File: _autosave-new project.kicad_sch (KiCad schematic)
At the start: 4 parts, among them J1 LED 0.170amps, J2 Tractive Battery

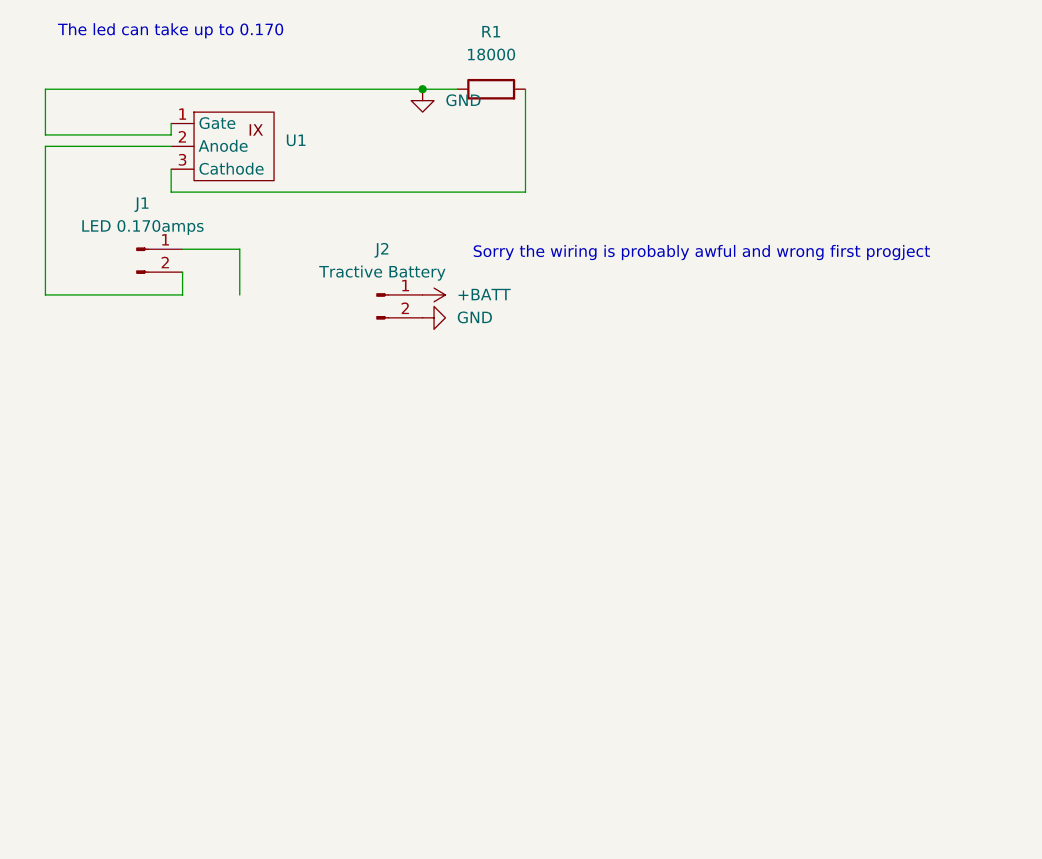
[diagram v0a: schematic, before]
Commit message: Check
Redoing Wiring
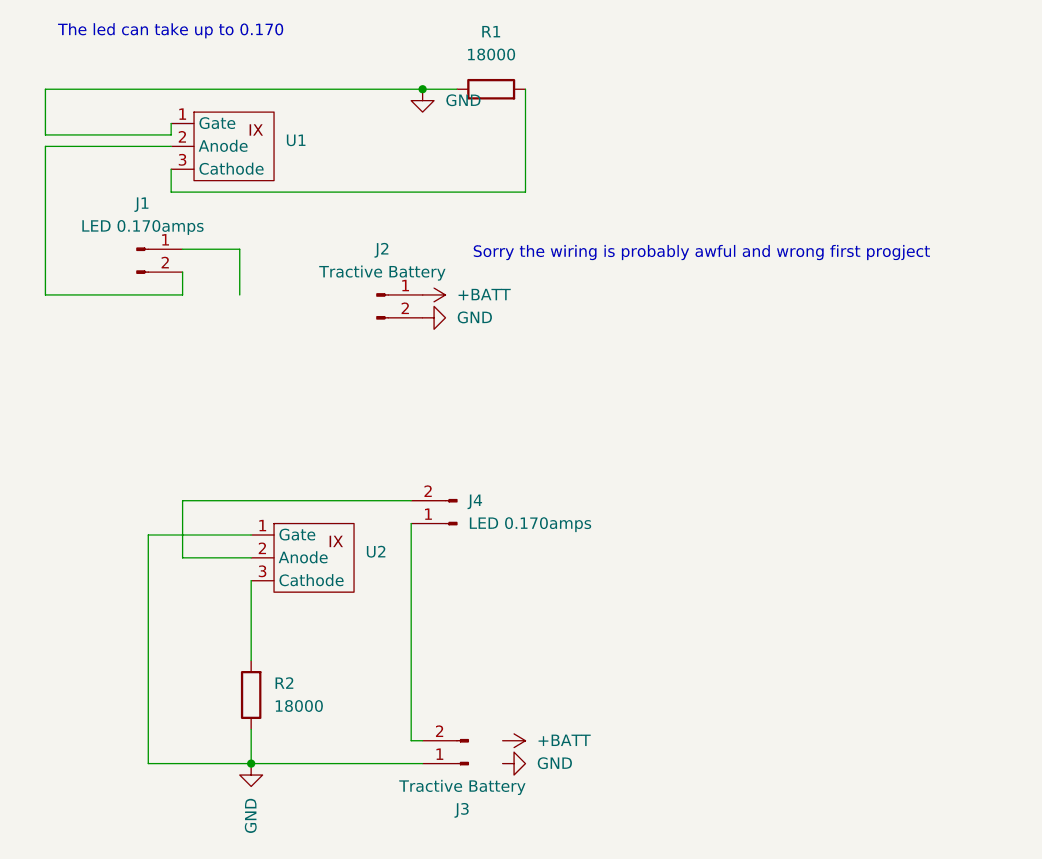
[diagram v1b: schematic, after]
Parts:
- added J3: Tractive Battery, Connector_Molex:Molex_Micro-Fit_3.0_43650-0200_1x02_P3.00mm_Horizontal, symbol Connector:Conn_01x02_Pin
- added J4: LED 0.170amps, Connector_Molex:Molex_Micro-Fit_3.0_43650-0200_1x02_P3.00mm_Horizontal, symbol Connector:Conn_01x02_Pin
- added R2: 18000, Resistor_THT:R_Axial_DIN0207_L6.3mm_D2.5mm_P15.24mm_Horizontal, symbol Device:R
- added U2: ~, Package_TO_SOT_SMD:TO-252-2, symbol IXCP10M90S:IXCP10M90S
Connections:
- net GND: now also J3.1 (Pin_1), R2.1, U2.1 (Gate)
- new net: R2.2, U2.3 (Cathode)
- new net: J3.2 (Pin_2), J4.1 (Pin_1)
- new net: J4.2 (Pin_2), U2.2 (Anode)
